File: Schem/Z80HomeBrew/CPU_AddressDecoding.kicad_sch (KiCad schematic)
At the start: 20 parts, among them U10 ATF22V10C-10PU, U11 74HC273, U30 74LS244, U6 AS7C4096A-12TCN, U7 ATF22V10C-10PU, U8 Z084000xP, U9 SST39SF040-70-4C-PHE

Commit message: Completed schematics
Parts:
- U11: value 74HC273 -> SN74HC273DWR
- U30: value 74LS244 -> SN74HC244DWR; footprint (none) -> Package_SO:SOIC-20W_7.5x12.8mm_P1.27mm
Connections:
- net D1: now also U7.14 (IO14)
- net ~{BUSREQ}: now also RN3.7 (R6); no longer RN3.8 (R7)
- net ~{RD}: now also RN3.4 (R3); no longer RN3.5 (R4)
- net ~{RESET}: now also RN3.8 (R7)
- net ~{WAIT}: now also RN3.6 (R5); no longer RN3.7 (R6)
- net ~{WR}: now also RN3.5 (R4); no longer RN3.6 (R5)
- net IEI: now reaches U7.11 (I11)
- net EXP_IEI: now reaches U7.15 (IO15)
- net ~{INT_VDP}: now reaches U7.9 (I9)
- net A16 renamed BANK_Q0
- net A17 renamed BANK_Q1
- net A18 renamed BANK_Q2
- no-connect marks 14 -> 9
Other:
- note added: "Read Buffer"
- note added: "Write Latch"
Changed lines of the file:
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@@
 	(generator_version "9.0")
 	(paper "USLedger")
+	(text "Write Latch"
+		(exclude_from_sim no)
+		(at 65.532 194.564 0)
+		(effects
+			(font
+				(size 1.27 1.27)
+			)
+		)
+	)
+	(text "Read Buffer"
+		(exclude_from_sim no)
+		(at 134.112 194.564 0)
+		(effects
+			(font
+				(size 1.27 1.27)
+			)
+		)
+	)
 	(text_box "Decoupling"
 		(exclude_from_sim no)
@@
 	)
 	(no_connect
-		(at 199.39 76.2)
-	)
-	(no_connect
-		(at 199.39 81.28)
-	)
-	(no_connect
-		(at 229.87 76.2)
-	)
-	(no_connect
 		(at 199.39 78.74)
 	)
 	(no_connect
-		(at 229.87 78.74)
-	)
-	(no_connect
 		(at 121.92 78.74)
 	)
@@
 	)
 	(no_connect
-		(at 121.92 76.2)
-	)
-	(no_connect
 		(at 121.92 81.28)
 	)
@@
 	(wire
 		(pts
+			(xy 186.69 81.28) (xy 199.39 81.28)
+		)
+		(stroke
+			(width 0)
+			(type default)
+		)
+	)
+	(wire
+		(pts
 			(xy 375.92 67.31) (xy 388.62 67.31)
 		)
@@
 	(wire
 		(pts
-			(xy 121.92 66.04) (xy 128.27 66.04)
+			(xy 121.92 68.58) (xy 128.27 68.58)
 		)
 		(stroke
@@
 	(wire
 		(pts
+			(xy 186.69 76.2) (xy 199.39 76.2)
+		)
+		(stroke
+			(width 0)
+			(type default)
+		)
+	)
+	(wire
+		(pts
 			(xy 71.12 166.37) (xy 88.9 166.37)
 		)
@@
 	(wire
 		(pts
-			(xy 121.92 71.12) (xy 128.27 71.12)
+			(xy 121.92 73.66) (xy 128.27 73.66)
 		)
 		(stroke
@@
 	(wire
 		(pts
-			(xy 121.92 68.58) (xy 128.27 68.58)
+			(xy 121.92 71.12) (xy 128.27 71.12)
 		)
 		(stroke
@@
 	(wire
 		(pts
+			(xy 121.92 66.04) (xy 128.27 66.04)
+		)
+		(stroke
+			(width 0)
+			(type default)
+		)
+	)
+	(wire
+		(pts
 			(xy 69.85 57.15) (xy 83.82 57.15)
 		)
@@
 	(wire
 		(pts
+			(xy 229.87 78.74) (xy 242.57 78.74)
+		)
+		(stroke
+			(width 0)
+			(type default)
+		)
+	)
+	(wire
+		(pts
 			(xy 121.92 43.18) (xy 128.27 43.18)
 		)
@@
 	(wire
 		(pts
-			(xy 121.92 73.66) (xy 128.27 73.66)
+			(xy 121.92 76.2) (xy 128.27 76.2)
 		)
 		(stroke
@@
 	(wire
 		(pts
+			(xy 229.87 76.2) (xy 242.57 76.2)
+		)
+		(stroke
+			(width 0)
+			(type default)
+		)
+	)
+	(wire
+		(pts
 			(xy 229.87 71.12) (xy 240.03 71.12)
 		)
@@
 	)
 	(label "~{RD}"
-		(at 128.27 73.66 180)
+		(at 128.27 76.2 180)
 		(effects
 			(font
@@
 	)
 	(label "~{WAIT}"
-		(at 128.27 68.58 180)
+		(at 128.27 71.12 180)
 		(effects
 			(font
@@
 		)
 	)
+	(label "~{RESET}"
+		(at 128.27 66.04 180)
+		(effects
+			(font
+				(size 1.27 1.27)
+			)
+			(justify right bottom)
+		)
+	)
 	(label "D4"
 		(at 372.11 189.23 180)
@@
 		)
 	)
-	(label "CLK"
-		(at 30.48 49.53 0)
-		(effects
-			(font
-				(size 1.27 1.27)
-			)
-			(justify left bottom)
-		)
-	)
 	(label "RAM_A16"
 		(at 388.62 59.69 180)
@@
 		)
 	)
+	(label "D1"
+		(at 242.57 78.74 180)
+		(effects
+			(font
+				(size 1.27 1.27)
+			)
+			(justify right bottom)
+		)
+	)
 	(label "~{IORQ}"
 		(at 186.69 63.5 0)
@@
 	)
 	(label "~{WR}"
-		(at 128.27 71.12 180)
+		(at 128.27 73.66 180)
 		(effects
 			(font
@@
 	)
 	(label "~{BUSREQ}"
-		(at 128.27 66.04 180)
+		(at 128.27 68.58 180)
 		(effects
 			(font
@@
 		)
 	)
-	(hierarchical_label "A18"
-		(shape output)
-		(at 88.9 168.91 0)
+	(hierarchical_label "IEI"
+		(shape input)
+		(at 186.69 81.28 180)
 		(effects
 			(font
 				(size 1.27 1.27)
 			)
-			(justify left)
+			(justify right)
 		)
 	)
@@
 		)
 	)
-	(hierarchical_label "A16"
-		(shape output)
-		(at 88.9 163.83 0)
-		(effects
-			(font
-				(size 1.27 1.27)
-			)
-			(justify left)
-		)
-	)
 	(hierarchical_label "~{BUSACK}"
 		(shape output)
@@
 	)
 	(hierarchical_label "~{BUSREQ}"
-		(shape input)
+		(shape passive)
 		(at 30.48 82.55 180)
 		(effects
@@
 	)
 	(hierarchical_label "~{INT}"
-		(shape input)
+		(shape passive)
 		(at 30.48 92.71 180)
 		(effects
@@
 		)
 	)
-	(hierarchical_label "A17"
-		(shape output)
-		(at 88.9 166.37 0)
-		(effects
-			(font
-				(size 1.27 1.27)
-			)
-			(justify left)
-		)
-	)
 	(hierarchical_label "~{CS_CART_IO}"
 		(shape output)
@@
 		)
 	)
-	(hierarchical_label "A[0..18]"
+	(hierarchical_label "A[0..15]"
 		(shape output)
 		(at 86.36 46.99 0)
@@
 		)
 	)
+	(hierarchical_label "~{MREQ}"
+		(shape output)
+		(at 30.48 62.23 180)
+		(effects
+			(font
+				(size 1.27 1.27)
+			)
+			(justify right)
+		)
+	)
 	(hierarchical_label "~{CART_CS}"
 		(shape output)
@@
 	)
 	(hierarchical_label "~{WAIT}"
-		(shape input)
+		(shape passive)
 		(at 30.48 102.87 180)
 		(effects
@@
 	)
 	(hierarchical_label "~{NMI}"
-		(shape input)
+		(shape passive)
 		(at 30.48 95.25 180)
 		(effects
@@
 		)
 	)
+	(hierarchical_label "~{INT_VDP}"
+		(shape input)
+		(at 186.69 76.2 180)
+		(effects
+			(font
+				(size 1.27 1.27)
+			)
+			(justify right)
+		)
+	)
 	(hierarchical_label "~{M1}"
 		(shape output)
@@
 		)
 	)
-	(hierarchical_label "D[0..8]"
+	(hierarchical_label "EXP_IEI"
+		(shape output)
+		(at 242.57 76.2 0)
+		(effects
+			(font
+				(size 1.27 1.27)
+			)
+			(justify left)
+		)
+	)
+	(hierarchical_label "D[0..7]"
 		(shape bidirectional)
 		(at 152.4 161.29 0)
@@
 		)
 	)
-	(hierarchical_label "D[0..8]"
+	(hierarchical_label "D[0..7]"
 		(shape bidirectional)
 		(at 29.21 161.29 180)
@@
 		)
 	)
-	(hierarchical_label "D[0..8]"
+	(hierarchical_label "D[0..7]"
 		(shape bidirectional)
 		(at 86.36 90.17 0)
@@
 			)
 		)
-		(property "Value" "74HC273"
+		(property "Value" "SN74HC273DWR"
 			(at 60.5633 158.75 0)
 			(effects
@@
 	)
 	(symbol
+		(lib_name "PEEL22CV10AP_1")
 		(lib_id "Logic_Programmable:PEEL22CV10AP")
 		(at 214.63 68.58 0)
@@
 			)
 		)
-		(property "Value" "74LS244"
+		(property "Value" "SN74HC244DWR"
 			(at 129.1433 158.75 0)
 			(effects
@@
 			)
 		)
-		(property "Footprint" ""
+		(property "Footprint" "Package_SO:SOIC-20W_7.5x12.8mm_P1.27mm"
 			(at 127 176.53 0)
 			(effects

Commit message: Finally found a name "Zephyr-80" for the brew and committing the first pbc
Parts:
- added C67: 100n, Capacitor_SMD:C_0805_2012Metric, symbol Device:C
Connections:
- net +5V: now also C67.1
- net GND: now also C67.2
- net ~{BUSREQ}: now also RN3.5 (R4); no longer RN3.7 (R6)
- net ~{RD}: now also RN3.2 (R1); no longer RN3.4 (R3)
- net ~{RESET}: now also RN3.6 (R5); no longer RN3.8 (R7)
- net ~{WAIT}: now also RN3.4 (R3); no longer RN3.6 (R5)
- net ~{WR}: now also RN3.3 (R2); no longer RN3.5 (R4)
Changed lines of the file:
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@@
 	)
 	(junction
+		(at 113.03 232.41)
+		(diameter 0)
+		(color 0 0 0 0)
+	)
+	(junction
 		(at 101.6 248.92)
 		(diameter 0)
@@
 	)
 	(junction
+		(at 113.03 248.92)
+		(diameter 0)
+		(color 0 0 0 0)
+	)
+	(junction
 		(at 182.88 167.64)
 		(diameter 0)
@@
 	)
 	(no_connect
-		(at 121.92 78.74)
-	)
-	(no_connect
 		(at 231.14 162.56)
 	)
@@
 	)
 	(no_connect
+		(at 121.92 68.58)
+	)
+	(no_connect
 		(at 121.92 50.8)
 	)
 	(no_connect
-		(at 121.92 81.28)
+		(at 121.92 66.04)
 	)
 	(bus_entry
@@
 	(wire
 		(pts
-			(xy 121.92 68.58) (xy 128.27 68.58)
+			(xy 121.92 73.66) (xy 128.27 73.66)
 		)
 		(stroke
@@
 	(wire
 		(pts
-			(xy 121.92 73.66) (xy 128.27 73.66)
+			(xy 121.92 78.74) (xy 128.27 78.74)
 		)
 		(stroke
@@
 	(wire
 		(pts
-			(xy 121.92 71.12) (xy 128.27 71.12)
+			(xy 121.92 76.2) (xy 128.27 76.2)
 		)
 		(stroke
@@
 	(wire
 		(pts
-			(xy 121.92 66.04) (xy 128.27 66.04)
+			(xy 121.92 71.12) (xy 128.27 71.12)
 		)
 		(stroke
@@
 	(wire
 		(pts
+			(xy 124.46 236.22) (xy 124.46 232.41)
+		)
+		(stroke
+			(width 0)
+			(type default)
+		)
+	)
+	(wire
+		(pts
 			(xy 31.75 173.99) (xy 45.72 173.99)
 		)
@@
 		)
 	)
+	(wire
+		(pts
+			(xy 124.46 243.84) (xy 124.46 248.92)
+		)
+		(stroke
+			(width 0)
+			(type default)
+		)
+	)
 	(bus
 		(pts
@@
 	(wire
 		(pts
+			(xy 113.03 232.41) (xy 124.46 232.41)
+		)
+		(stroke
+			(width 0)
+			(type default)
+		)
+	)
+	(wire
+		(pts
 			(xy 43.18 248.92) (xy 55.88 248.92)
 		)
@@
 	(wire
 		(pts
+			(xy 101.6 248.92) (xy 113.03 248.92)
+		)
+		(stroke
+			(width 0)
+			(type default)
+		)
+	)
+	(wire
+		(pts
 			(xy 149.86 81.28) (xy 156.21 81.28)
 		)
@@
 	(wire
 		(pts
+			(xy 113.03 248.92) (xy 124.46 248.92)
+		)
+		(stroke
+			(width 0)
+			(type default)
+		)
+	)
+	(wire
+		(pts
 			(xy 77.47 243.84) (xy 77.47 248.92)
 		)
@@
 		)
 	)
-	(wire
-		(pts
-			(xy 101.6 248.92) (xy 113.03 248.92)
-		)
-		(stroke
-			(width 0)
-			(type default)
-		)
-	)
 	(bus
 		(pts
@@
 	(wire
 		(pts
-			(xy 121.92 76.2) (xy 128.27 76.2)
+			(xy 121.92 81.28) (xy 128.27 81.28)
 		)
 		(stroke
@@
 	)
 	(label "~{RD}"
-		(at 128.27 76.2 180)
+		(at 128.27 81.28 180)
 		(effects
 			(font
@@
 	)
 	(label "~{WAIT}"
-		(at 128.27 71.12 180)
+		(at 128.27 76.2 180)
 		(effects
 			(font
@@
 	)
 	(label "~{RESET}"
-		(at 128.27 66.04 180)
+		(at 128.27 71.12 180)
 		(effects
 			(font
@@
 	)
 	(label "~{WR}"
-		(at 128.27 73.66 180)
+		(at 128.27 78.74 180)
 		(effects
 			(font
@@
 	)
 	(label "~{BUSREQ}"
-		(at 128.27 68.58 180)
+		(at 128.27 73.66 180)
 		(effects
 			(font
@@
 					(unit 1)
 				)
+			)
+		)
+	)
+	(symbol
+		(lib_id "Device:C")
+		(at 124.46 240.03 0)
+		(unit 1)
+		(exclude_from_sim no)
+		(in_bom yes)
+		(on_board yes)
+		(dnp no)
+		(fields_autoplaced yes)
+		(property "Reference" "C67"
+			(at 128.27 238.7599 0)
+			(effects
+				(font
+					(size 1.27 1.27)
+				)
+				(justify left)
+			)
+		)
+		(property "Value" "100n"
+			(at 128.27 241.2999 0)
+			(effects
+				(font
+					(size 1.27 1.27)
+				)
+				(justify left)
+			)
+		)
+		(property "Footprint" "Capacitor_SMD:C_0805_2012Metric"
+			(at 125.4252 243.84 0)
+			(effects
+				(font
+					(size 1.27 1.27)
+				)
+				(hide yes)
+			)
+		)
+		(property "Datasheet" "~"
+			(at 124.46 240.03 0)
+			(effects
+				(font
+					(size 1.27 1.27)
+				)
+				(hide yes)
+			)
+		)
+		(property "Description" "Unpolarized capacitor"
+			(at 124.46 240.03 0)
+			(effects
+				(font
+					(size 1.27 1.27)
+				)
+				(hide yes)
+			)
+		)
+		(pin "1"
+		)
+		(pin "2"
+		)
+		(instances
+			(project "Z80HomeBrew"
+				(path "/5593e793-d133-45d0-a91e-72805049e474/42f260a1-43d6-4f51-bd99-df380e29398c"
+					(reference "C67")
+					(unit 1)
+				)

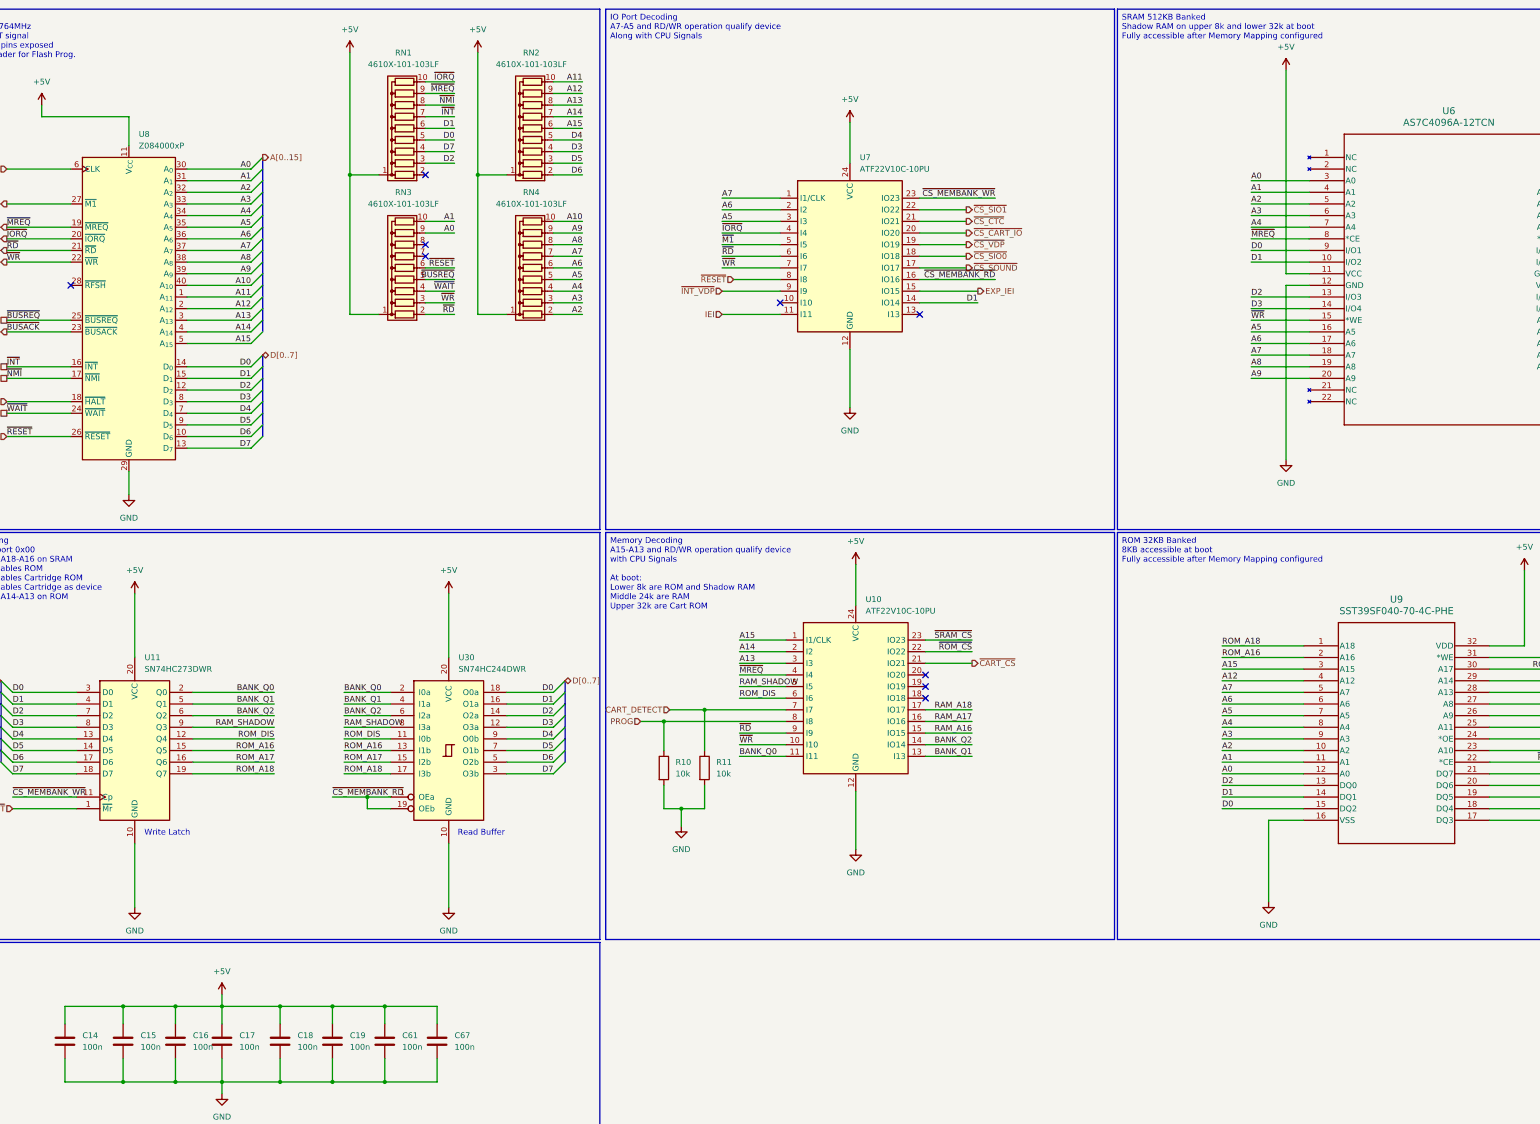
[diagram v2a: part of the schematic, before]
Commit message: Added pBITzBackplane and MezzanineConnector
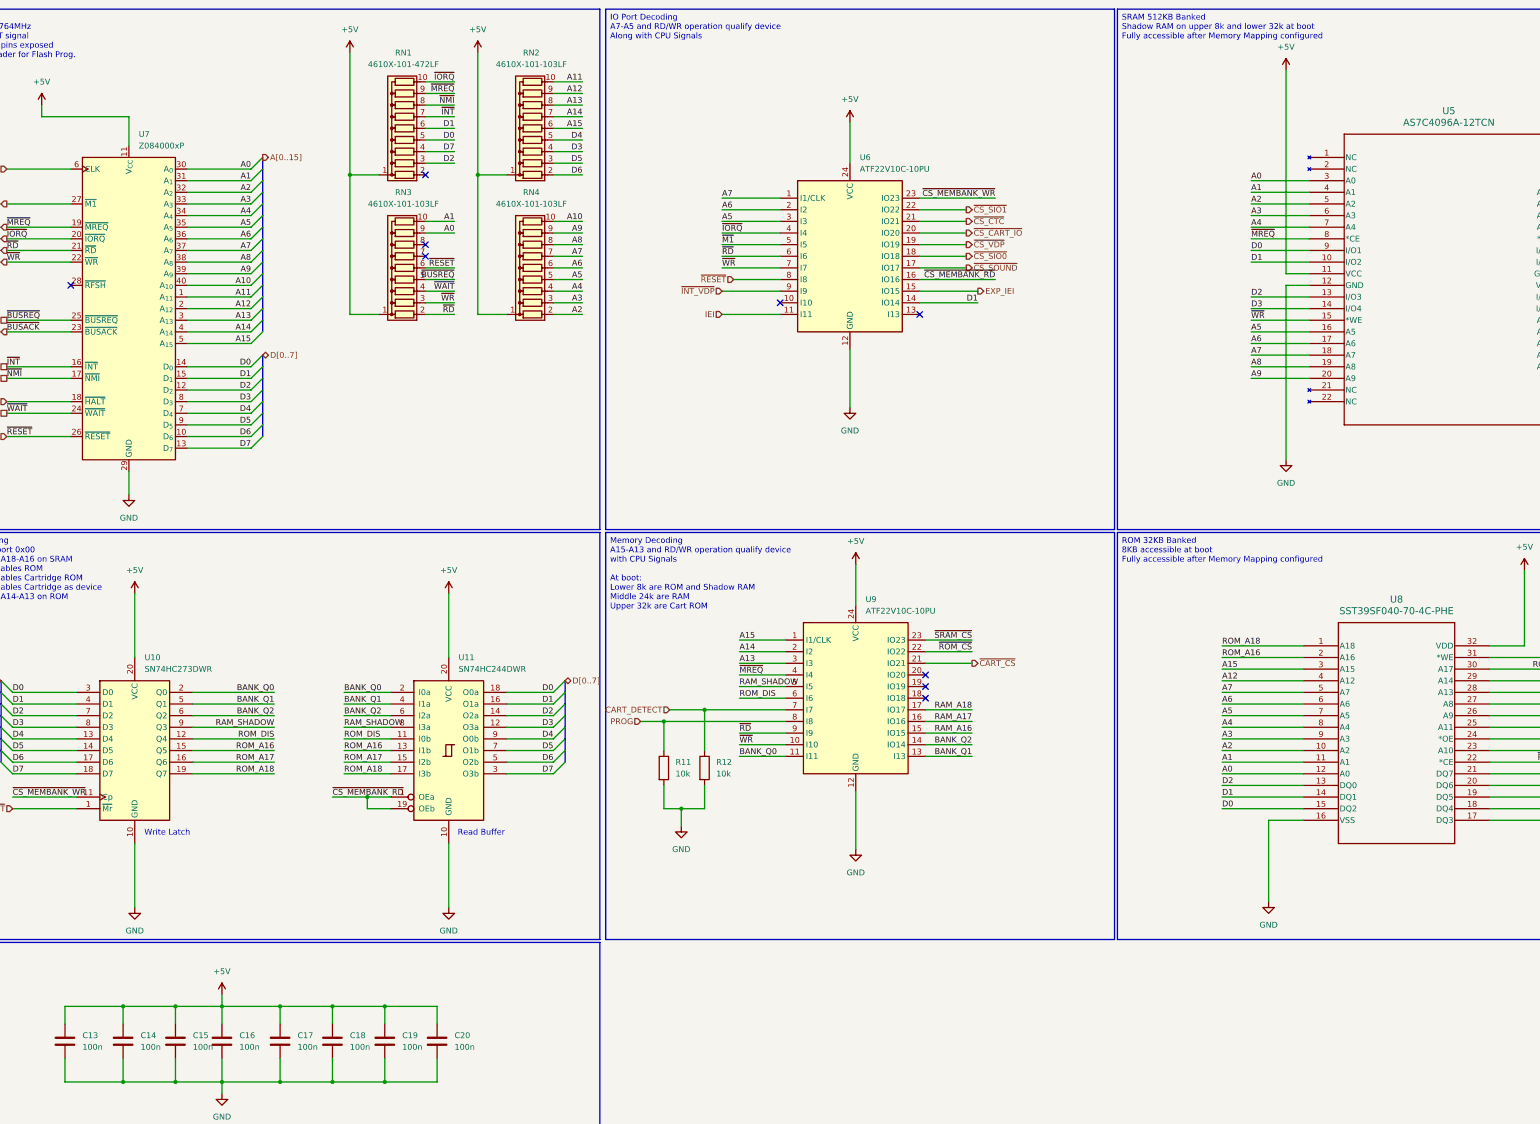
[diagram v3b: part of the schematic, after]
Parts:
- C13: renamed from C14; MANUFACTURER_PART_NUMBER (none) -> 0402B104K160CT
- C14: renamed from C15; MANUFACTURER_PART_NUMBER (none) -> 0402B104K160CT
- C15: renamed from C16; MANUFACTURER_PART_NUMBER (none) -> 0402B104K160CT
- C16: renamed from C17; MANUFACTURER_PART_NUMBER (none) -> 0402B104K160CT
- C17: renamed from C18; MANUFACTURER_PART_NUMBER (none) -> 0402B104K160CT
- C18: renamed from C19; MANUFACTURER_PART_NUMBER (none) -> 0402B104K160CT
- C19: renamed from C61; MANUFACTURER_PART_NUMBER (none) -> 0402B104K160CT
- C20: renamed from C67; MANUFACTURER_PART_NUMBER (none) -> 0402B104K160CT
- R11: renamed from R10; MANUFACTURER_PART_NUMBER (none) -> RC0603FR-0710KL
- R12: renamed from R11; MANUFACTURER_PART_NUMBER (none) -> RC0603FR-0710KL
- RN1: value 4610X-101-103LF -> 4610X-101-472LF; MANUFACTURER_PART_NUMBER (none) -> 4610X-101-103LF
- RN2, RN3, RN4: MANUFACTURER_PART_NUMBER (none) -> 4610X-101-103LF
- U10: renamed from U11; MANUFACTURER_PART_NUMBER (none) -> SN74HC273DWR
- U11: renamed from U30; MANUFACTURER_PART_NUMBER (none) -> SN74HC244DWR
- U5: renamed from U6; MANUFACTURER_PART_NUMBER (none) -> AS7C4096A-12TCN
- U6: renamed from U7; MANUFACTURER_PART_NUMBER (none) -> ATF22V10C-10PU
- U7: renamed from U8; MANUFACTURER_PART_NUMBER (none) -> A 40-LC-TT
- U8: renamed from U9; MANUFACTURER_PART_NUMBER (none) -> SST39SF040-70-4C-PHE
- U9: renamed from U10; MANUFACTURER_PART_NUMBER (none) -> ATF22V10C-10PU
